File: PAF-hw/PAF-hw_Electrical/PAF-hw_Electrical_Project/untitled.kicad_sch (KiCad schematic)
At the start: 7 parts, among them IC2 NCP1117IST33T3G

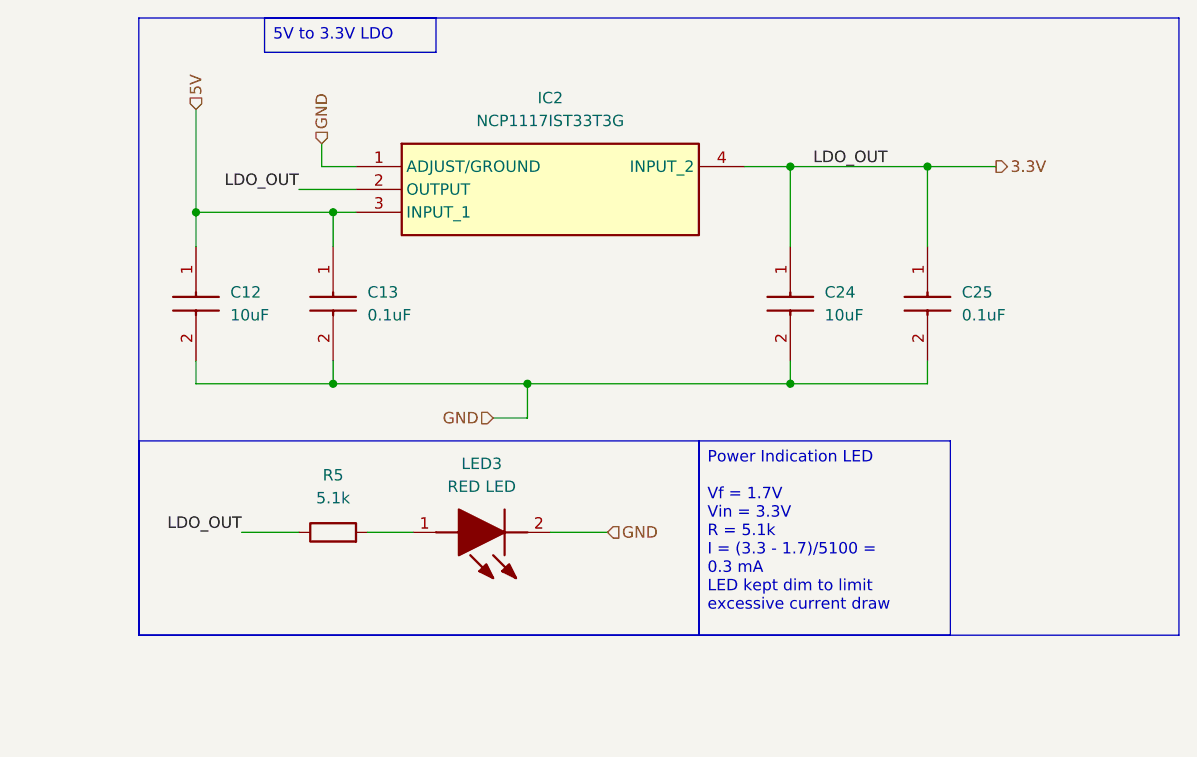
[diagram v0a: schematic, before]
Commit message: Added camera circuit to schematic.
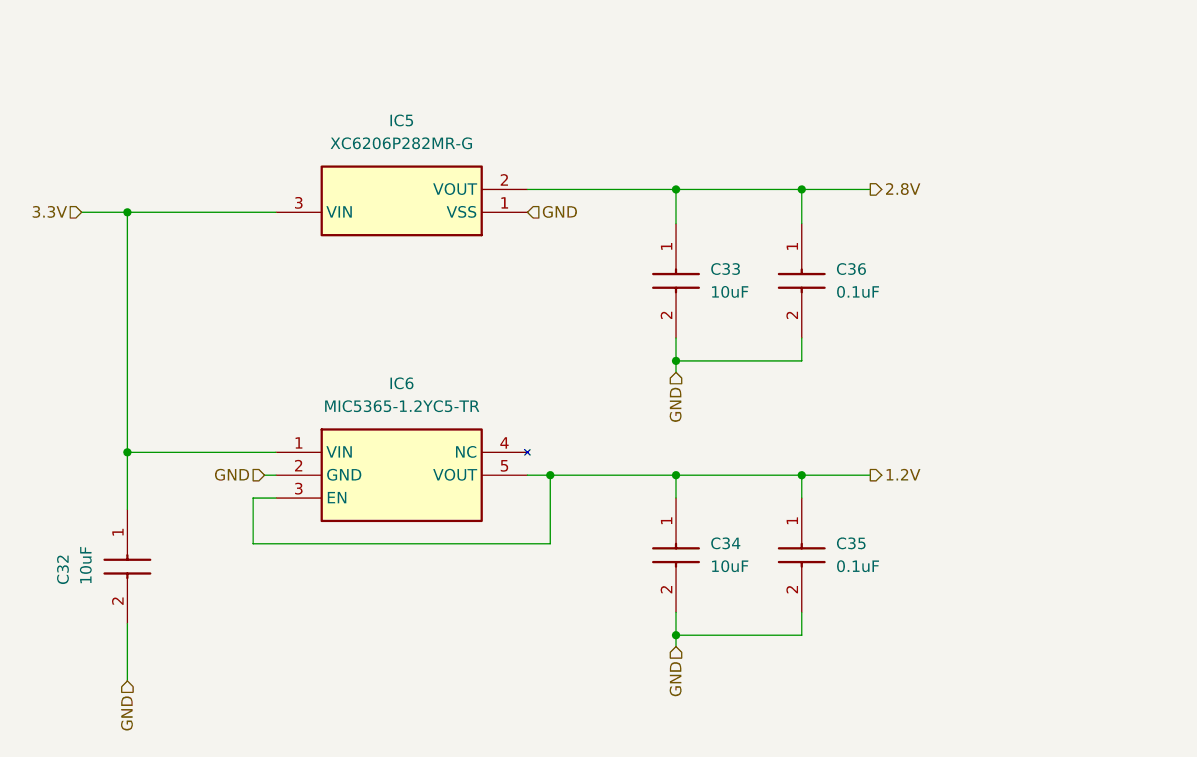
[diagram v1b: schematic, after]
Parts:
- removed C12, C24: 10uF, CAPC2012X145N, symbol SamacSys_Parts:CL21A106KAYNNNE
- removed C13, C25: 0.1uF, C0603, symbol SamacSys_Parts:C0603C104K5RACTU
- removed IC2: NCP1117IST33T3G, SOT230P700X180-4N, symbol SamacSys_Parts:NCP1117IST33T3G
- removed LED3: RED LED, SMLLX0805SRCTR, symbol SamacSys_Parts:SML-LX0805SRC-TR
- removed R5: 5.1k, symbol Device:R
- added C32, C33, C34: 10uF, CAPC2012X145N, symbol SamacSys_Parts:CL21A106KAYNNNE
- added C35, C36: 0.1uF, C0603, symbol SamacSys_Parts:C0603C104K5RACTU
- added IC5: XC6206P282MR-G, SOT95P280X130-3N, symbol SamacSys_Parts:XC6206P282MR-G
- added IC6: MIC5365-1.2YC5-TR, SOT65P210X110-5N, symbol SamacSys_Parts:MIC5365-1.2YC5-TR
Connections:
- net 3.3V: now also C32.1, IC5.3 (VIN), IC6.1 (VIN)
- net GND: now also C32.2, C33.2, C34.2, C35.2, C36.2, IC5.1 (VSS), IC6.2 (GND)
- new net 1.2V: C34.1, C35.1, IC6.3 (EN), IC6.5 (VOUT)
- new net 2.8V: C33.1, C36.1, IC5.2 (VOUT)
